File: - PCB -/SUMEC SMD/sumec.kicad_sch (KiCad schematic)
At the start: 0 parts

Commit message: PCB SMD update
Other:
- title: SUMEC THT -> SUMEC SMD
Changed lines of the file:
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@@
   (paper "A4")
   (title_block
-    (title "SUMEC THT")
+    (title "SUMEC SMD")
     (company "SPŠ NA PROSEKU")
   )

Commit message: LOGO LETSS GGOOO WOOAH YEAAAAH
holy moly logo darg wizzarddry shit, its so fire LETSS GOOO
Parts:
- added R1: R, LOGO:some magic shit (logo), symbol Device:R
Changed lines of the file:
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@@
     (company "SPŠ NA PROSEKU")
   )
-  (sheet (at 21.59 83.82) (size 69.85 46.99)
+  (symbol (lib_id "some magic shit (logo):LOGO") (at 140.97 29.21 0) (unit 1)
+    (in_bom yes) (on_board yes) (dnp no) (fields_autoplaced)
+    (property "Reference" "#G1" (at 140.97 18.5843 0)
+      (effects (font (size 1.27 1.27)) hide)
+    )
+    (property "Value" "LOGO" (at 140.97 39.8357 0)
+      (effects (font (size 1.27 1.27)) hide)
+    )
+    (property "Footprint" "LOGO:some magic shit (logo)" (at 140.97 29.21 0)
+      (effects (font (size 1.27 1.27)) hide)
+    )
+    (property "Datasheet" "" (at 140.97 29.21 0)
+      (effects (font (size 1.27 1.27)) hide)
+    )
+    (instances
+      (project "sumec"
+        (path "/fc70a1a8-ed7c-4a0f-9b1a-f23293528385"
+          (reference "#G1") (unit 1)
+        )
+      )
+    )
+  )
+  (symbol (lib_id "Device:R") (at 185.42 27.94 0) (unit 1)
+    (in_bom yes) (on_board yes) (dnp no) (fields_autoplaced)
+    (property "Reference" "R1" (at 187.96 27.305 0)
+      (effects (font (size 1.27 1.27)) (justify left))
+    )
+    (property "Value" "R" (at 187.96 29.845 0)
+      (effects (font (size 1.27 1.27)) (justify left))
+    )
+    (property "Footprint" "LOGO:some magic shit (logo)" (at 183.642 27.94 90)
+      (effects (font (size 1.27 1.27)) hide)
+    )
+    (property "Datasheet" "~" (at 185.42 27.94 0)
+      (effects (font (size 1.27 1.27)) hide)
+    )
+    (pin "1")
+    (pin "2")
+    (instances
+      (project "sumec"
+        (path "/fc70a1a8-ed7c-4a0f-9b1a-f23293528385"
+          (reference "R1") (unit 1)
+        )
+      )
+    )
+  )
+  (sheet (at 22.86 110.49) (size 69.85 46.99)
     (stroke (width 0.1524) (type solid) (color 0 0 0 1))
     (fill (color 255 255 255 1.0000))
-    (property "Sheetname" "MECHANICS" (at 33.02 110.49 0)
+    (property "Sheetname" "MECHANICS" (at 34.29 137.16 0)
       (effects (font (size 5 5) bold (color 0 0 0 1)) (justify left bottom))
     )
-    (property "Sheetfile" "MECHANICS.kicad_sch" (at 21.59 132.08 0)
+    (property "Sheetfile" "MECHANICS.kicad_sch" (at 22.86 158.75 0)
       (effects (font (size 1.27 1.27) (color 0 0 0 1)) (justify left top))
     )
@@
     )
   )
-  (sheet (at 20.32 21.59) (size 69.85 46.99)
+  (sheet (at 22.86 53.34) (size 69.85 46.99)
     (stroke (width 0.1524) (type solid) (color 0 0 0 1))
     (fill (color 255 255 255 1.0000))
-    (property "Sheetname" "MCU" (at 45.72 46.99 0)
+    (property "Sheetname" "MCU" (at 48.26 78.74 0)
       (effects (font (size 5 5) bold (color 0 0 0 1)) (justify left bottom))
     )
-    (property "Sheetfile" "MCU.kicad_sch" (at 20.32 69.85 0)
+    (property "Sheetfile" "MCU.kicad_sch" (at 22.86 101.6 0)
       (effects (font (size 1.27 1.27) (color 0 0 0 1)) (justify left top))
     )
@@
     )
   )
-  (sheet (at 196.85 21.59) (size 69.85 46.99)
+  (sheet (at 199.39 53.34) (size 69.85 46.99)
     (stroke (width 0.1524) (type solid) (color 0 0 0 1))
     (fill (color 255 255 255 1.0000))
-    (property "Sheetname" "POWER SUPPLY" (at 201.93 46.99 0)
+    (property "Sheetname" "POWER SUPPLY" (at 204.47 78.74 0)
       (effects (font (size 5 5) bold (color 0 0 0 1)) (justify left bottom))
     )
-    (property "Sheetfile" "POWER SUPPLY.kicad_sch" (at 196.85 69.85 0)
+    (property "Sheetfile" "POWER SUPPLY.kicad_sch" (at 199.39 101.6 0)
       (effects (font (size 1.27 1.27) (color 0 0 0 1)) (justify left top))
     )
@@
     )
   )
-  (sheet (at 107.95 21.59) (size 69.85 46.99)
+  (sheet (at 110.49 53.34) (size 69.85 46.99)
     (stroke (width 0.1524) (type solid) (color 0 0 0 1))
     (fill (color 255 255 255 1.0000))
-    (property "Sheetname" "SENSORS" (at 125.73 46.99 0)
+    (property "Sheetname" "SENSORS" (at 128.27 78.74 0)
       (effects (font (size 5 5) bold (color 0 0 0 1)) (justify left bottom))
     )
-    (property "Sheetfile" "SENSORS.kicad_sch" (at 107.95 69.1646 0)
+    (property "Sheetfile" "SENSORS.kicad_sch" (at 110.49 100.9146 0)
       (effects (font (size 1.27 1.27) (color 0 0 0 1)) (justify left top))
     )
-    (property "Field2" "" (at 107.95 21.59 0)
+    (property "Field2" "" (at 110.49 53.34 0)
       (effects (font (size 1.27 1.27)) hide)
     )

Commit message: PCB SMD update
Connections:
- no-connect marks 0 -> 2
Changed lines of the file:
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@@
     (company "SPŠ NA PROSEKU")
+  )
+  (no_connect (at 158.75 40.64))
+  (no_connect (at 130.81 40.64))
+  (wire (pts (xy 158.75 40.64) (xy 148.59 40.64))
+    (stroke (width 0) (type default))
+  )
+  (wire (pts (xy 130.81 40.64) (xy 140.97 40.64))
+    (stroke (width 0) (type default))
   )
   (symbol (lib_id "some magic shit (logo):LOGO") (at 140.97 29.21 0) (unit 1)
@@
     )
   )
-  (symbol (lib_id "Device:R") (at 185.42 27.94 0) (unit 1)
-    (in_bom yes) (on_board yes) (dnp no) (fields_autoplaced)
-    (property "Reference" "R1" (at 187.96 27.305 0)
-      (effects (font (size 1.27 1.27)) (justify left))
+  (symbol (lib_id "Device:R") (at 144.78 40.64 270) (mirror x) (unit 1)
+    (in_bom yes) (on_board yes) (dnp no)
+    (property "Reference" "R1" (at 145.415 38.1 0)
+      (effects (font (size 1.27 1.27)) (justify left) hide)
     )
-    (property "Value" "R" (at 187.96 29.845 0)
-      (effects (font (size 1.27 1.27)) (justify left))
+    (property "Value" "R" (at 142.875 38.1 0)
+      (effects (font (size 1.27 1.27)) (justify left) hide)
     )
-    (property "Footprint" "LOGO:some magic shit (logo)" (at 183.642 27.94 90)
+    (property "Footprint" "LOGO:some magic shit (logo)" (at 144.78 42.418 90)
       (effects (font (size 1.27 1.27)) hide)
     )
-    (property "Datasheet" "~" (at 185.42 27.94 0)
+    (property "Datasheet" "~" (at 144.78 40.64 0)
       (effects (font (size 1.27 1.27)) hide)
     )

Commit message: PCB smd - schematic update
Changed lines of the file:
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@@
     (company "SPŠ NA PROSEKU")
   )
-  (no_connect (at 158.75 40.64))
-  (no_connect (at 130.81 40.64))
-  (wire (pts (xy 158.75 40.64) (xy 148.59 40.64))
+  (no_connect (at 168.91 39.37))
+  (no_connect (at 140.97 39.37))
+  (wire (pts (xy 168.91 39.37) (xy 158.75 39.37))
     (stroke (width 0) (type default))
   )
-  (wire (pts (xy 130.81 40.64) (xy 140.97 40.64))
+  (wire (pts (xy 140.97 39.37) (xy 151.13 39.37))
     (stroke (width 0) (type default))
   )
-  (symbol (lib_id "some magic shit (logo):LOGO") (at 140.97 29.21 0) (unit 1)
+  (symbol (lib_id "some magic shit (logo):LOGO") (at 146.05 30.48 0) (unit 1)
     (in_bom yes) (on_board yes) (dnp no) (fields_autoplaced)
-    (property "Reference" "#G1" (at 140.97 18.5843 0)
+    (property "Reference" "#G1" (at 146.05 19.8543 0)
       (effects (font (size 1.27 1.27)) hide)
     )
-    (property "Value" "LOGO" (at 140.97 39.8357 0)
+    (property "Value" "LOGO" (at 146.05 41.1057 0)
       (effects (font (size 1.27 1.27)) hide)
     )
-    (property "Footprint" "LOGO:some magic shit (logo)" (at 140.97 29.21 0)
+    (property "Footprint" "LOGO:some magic shit (logo)" (at 146.05 30.48 0)
       (effects (font (size 1.27 1.27)) hide)
     )
-    (property "Datasheet" "" (at 140.97 29.21 0)
+    (property "Datasheet" "" (at 146.05 30.48 0)
       (effects (font (size 1.27 1.27)) hide)
     )
@@
     )
   )
-  (symbol (lib_id "Device:R") (at 144.78 40.64 270) (mirror x) (unit 1)
+  (symbol (lib_id "Device:R") (at 154.94 39.37 270) (mirror x) (unit 1)
     (in_bom yes) (on_board yes) (dnp no)
-    (property "Reference" "R1" (at 145.415 38.1 0)
+    (property "Reference" "R1" (at 155.575 36.83 0)
       (effects (font (size 1.27 1.27)) (justify left) hide)
     )
-    (property "Value" "R" (at 142.875 38.1 0)
+    (property "Value" "R" (at 153.035 36.83 0)
       (effects (font (size 1.27 1.27)) (justify left) hide)
     )
-    (property "Footprint" "LOGO:some magic shit (logo)" (at 144.78 42.418 90)
+    (property "Footprint" "LOGO:some magic shit (logo)" (at 154.94 41.148 90)
       (effects (font (size 1.27 1.27)) hide)
     )
-    (property "Datasheet" "~" (at 144.78 40.64 0)
+    (property "Datasheet" "~" (at 154.94 39.37 0)
       (effects (font (size 1.27 1.27)) hide)
     )
@@
     )
   )
-  (sheet (at 22.86 110.49) (size 69.85 46.99)
+  (sheet (at 27.94 107.95) (size 69.85 46.99)
     (stroke (width 0.1524) (type solid) (color 0 0 0 1))
     (fill (color 255 255 255 1.0000))
-    (property "Sheetname" "MECHANICS" (at 34.29 137.16 0)
+    (property "Sheetname" "MECHANICS" (at 39.37 134.62 0)
       (effects (font (size 5 5) bold (color 0 0 0 1)) (justify left bottom))
     )
-    (property "Sheetfile" "MECHANICS.kicad_sch" (at 22.86 158.75 0)
+    (property "Sheetfile" "MECHANICS.kicad_sch" (at 27.94 156.21 0)
       (effects (font (size 1.27 1.27) (color 0 0 0 1)) (justify left top))
     )
@@
     )
   )
-  (sheet (at 22.86 53.34) (size 69.85 46.99)
+  (sheet (at 27.94 49.53) (size 69.85 46.99)
     (stroke (width 0.1524) (type solid) (color 0 0 0 1))
     (fill (color 255 255 255 1.0000))
-    (property "Sheetname" "MCU" (at 48.26 78.74 0)
+    (property "Sheetname" "MCU" (at 53.34 74.93 0)
       (effects (font (size 5 5) bold (color 0 0 0 1)) (justify left bottom))
     )
-    (property "Sheetfile" "MCU.kicad_sch" (at 22.86 101.6 0)
+    (property "Sheetfile" "MCU.kicad_sch" (at 27.94 97.79 0)
       (effects (font (size 1.27 1.27) (color 0 0 0 1)) (justify left top))
     )
@@
     )
   )
-  (sheet (at 199.39 53.34) (size 69.85 46.99)
+  (sheet (at 204.47 49.53) (size 69.85 46.99)
     (stroke (width 0.1524) (type solid) (color 0 0 0 1))
     (fill (color 255 255 255 1.0000))
-    (property "Sheetname" "POWER SUPPLY" (at 204.47 78.74 0)
+    (property "Sheetname" "POWER SUPPLY" (at 209.55 74.93 0)
       (effects (font (size 5 5) bold (color 0 0 0 1)) (justify left bottom))
     )
-    (property "Sheetfile" "POWER SUPPLY.kicad_sch" (at 199.39 101.6 0)
+    (property "Sheetfile" "POWER SUPPLY.kicad_sch" (at 204.47 97.79 0)
       (effects (font (size 1.27 1.27) (color 0 0 0 1)) (justify left top))
     )
@@
     )
   )
-  (sheet (at 110.49 53.34) (size 69.85 46.99)
+  (sheet (at 115.57 49.53) (size 69.85 46.99)
     (stroke (width 0.1524) (type solid) (color 0 0 0 1))
     (fill (color 255 255 255 1.0000))
-    (property "Sheetname" "SENSORS" (at 128.27 78.74 0)
+    (property "Sheetname" "SENSORS" (at 133.35 74.93 0)
       (effects (font (size 5 5) bold (color 0 0 0 1)) (justify left bottom))
     )
-    (property "Sheetfile" "SENSORS.kicad_sch" (at 110.49 100.9146 0)
+    (property "Sheetfile" "SENSORS.kicad_sch" (at 115.57 97.1046 0)
       (effects (font (size 1.27 1.27) (color 0 0 0 1)) (justify left top))
     )
-    (property "Field2" "" (at 110.49 53.34 0)
+    (property "Field2" "" (at 115.57 49.53 0)
       (effects (font (size 1.27 1.27)) hide)
     )

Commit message: PCB update
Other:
- added sheet EXTERNAL (EXTERNAL.kicad_sch)
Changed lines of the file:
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@@
     )
   )
-  (sheet (at 27.94 107.95) (size 69.85 46.99)
+  (sheet (at 27.94 106.68) (size 69.85 46.99)
     (stroke (width 0.1524) (type solid) (color 0 0 0 1))
     (fill (color 255 255 255 1.0000))
-    (property "Sheetname" "MECHANICS" (at 39.37 134.62 0)
+    (property "Sheetname" "MECHANICS" (at 39.37 133.35 0)
       (effects (font (size 5 5) bold (color 0 0 0 1)) (justify left bottom))
     )
-    (property "Sheetfile" "MECHANICS.kicad_sch" (at 27.94 156.21 0)
+    (property "Sheetfile" "MECHANICS.kicad_sch" (at 27.94 154.94 0)
       (effects (font (size 1.27 1.27) (color 0 0 0 1)) (justify left top))
     )
@@
     )
   )
-  (sheet (at 27.94 49.53) (size 69.85 46.99)
+  (sheet (at 27.94 48.26) (size 69.85 46.99)
     (stroke (width 0.1524) (type solid) (color 0 0 0 1))
     (fill (color 255 255 255 1.0000))
-    (property "Sheetname" "MCU" (at 53.34 74.93 0)
+    (property "Sheetname" "MCU" (at 53.34 73.66 0)
       (effects (font (size 5 5) bold (color 0 0 0 1)) (justify left bottom))
     )
-    (property "Sheetfile" "MCU.kicad_sch" (at 27.94 97.79 0)
+    (property "Sheetfile" "MCU.kicad_sch" (at 27.94 96.52 0)
       (effects (font (size 1.27 1.27) (color 0 0 0 1)) (justify left top))
     )
@@
     )
   )
-  (sheet (at 204.47 49.53) (size 69.85 46.99)
+  (sheet (at 204.47 48.26) (size 69.85 46.99)
     (stroke (width 0.1524) (type solid) (color 0 0 0 1))
     (fill (color 255 255 255 1.0000))
-    (property "Sheetname" "POWER SUPPLY" (at 209.55 74.93 0)
+    (property "Sheetname" "POWER SUPPLY" (at 209.55 73.66 0)
       (effects (font (size 5 5) bold (color 0 0 0 1)) (justify left bottom))
     )
-    (property "Sheetfile" "POWER SUPPLY.kicad_sch" (at 204.47 97.79 0)
+    (property "Sheetfile" "POWER SUPPLY.kicad_sch" (at 204.47 96.52 0)
       (effects (font (size 1.27 1.27) (color 0 0 0 1)) (justify left top))
     )
@@
     )
   )
-  (sheet (at 115.57 49.53) (size 69.85 46.99)
+  (sheet (at 115.57 48.26) (size 69.85 46.99)
     (stroke (width 0.1524) (type solid) (color 0 0 0 1))
     (fill (color 255 255 255 1.0000))
-    (property "Sheetname" "SENSORS" (at 133.35 74.93 0)
+    (property "Sheetname" "SENSORS" (at 133.35 73.66 0)
       (effects (font (size 5 5) bold (color 0 0 0 1)) (justify left bottom))
     )
-    (property "Sheetfile" "SENSORS.kicad_sch" (at 115.57 97.1046 0)
+    (property "Sheetfile" "SENSORS.kicad_sch" (at 115.57 95.8346 0)
       (effects (font (size 1.27 1.27) (color 0 0 0 1)) (justify left top))
     )
-    (property "Field2" "" (at 115.57 49.53 0)
+    (property "Field2" "" (at 115.57 48.26 0)
       (effects (font (size 1.27 1.27)) hide)
     )
@@
       )
     )
+  )
+  (sheet (at 115.57 106.68) (size 69.85 46.99)
+    (stroke (width 0.1524) (type solid) (color 0 0 0 1))
+    (fill (color 255 255 255 1.0000))
+    (property "Sheetname" "EXTERNAL" (at 132.08 133.35 0)
+      (effects (font (size 5 5) bold (color 0 0 0 1)) (justify left bottom))
+    )
+    (property "Sheetfile" "EXTERNAL.kicad_sch" (at 115.57 154.2546 0)
+      (effects (font (size 1.27 1.27) (color 0 0 0 1)) (justify left top))
+    )
+    (instances
+      (project "sumec"
+        (path "/fc70a1a8-ed7c-4a0f-9b1a-f23293528385" (page "6"))
+      )
+    )

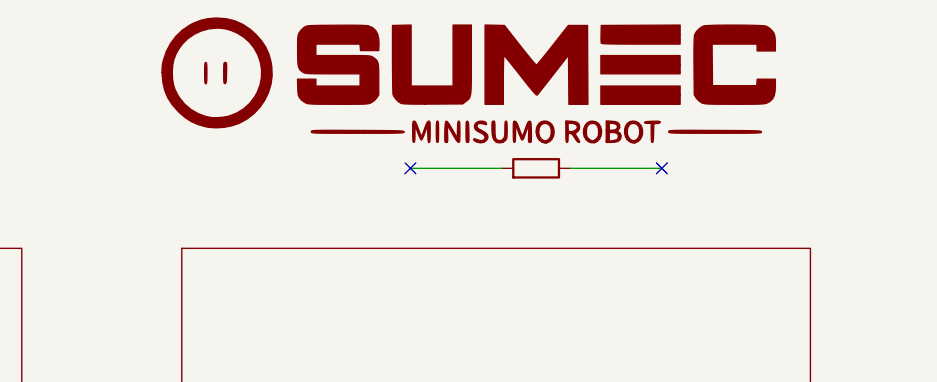
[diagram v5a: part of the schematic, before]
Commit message: PCB Update - "LIDAR"sensors
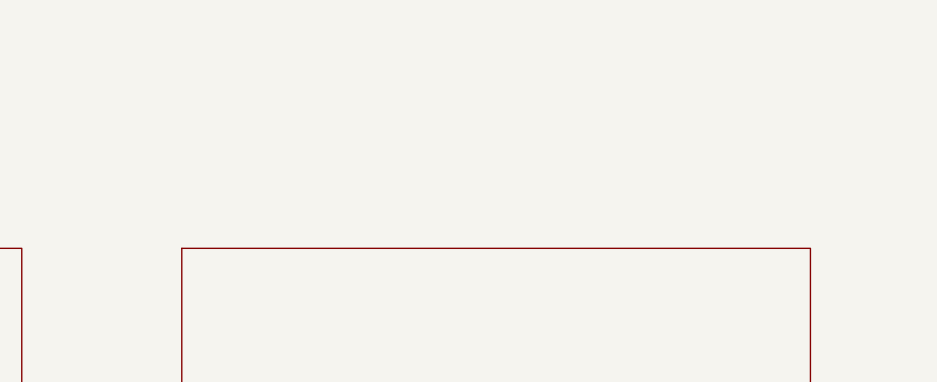
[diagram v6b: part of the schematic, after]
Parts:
- removed R1: R, LOGO:some magic shit (logo), symbol Device:R
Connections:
- no-connect marks 2 -> 0
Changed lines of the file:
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@@
     (company "SPŠ NA PROSEKU")
-  )
-  (no_connect (at 168.91 39.37))
-  (no_connect (at 140.97 39.37))
-  (wire (pts (xy 168.91 39.37) (xy 158.75 39.37))
-    (stroke (width 0) (type default))
-  )
-  (wire (pts (xy 140.97 39.37) (xy 151.13 39.37))
-    (stroke (width 0) (type default))
-  )
-  (symbol (lib_id "some magic shit (logo):LOGO") (at 146.05 30.48 0) (unit 1)
-    (in_bom yes) (on_board yes) (dnp no) (fields_autoplaced)
-    (property "Reference" "#G1" (at 146.05 19.8543 0)
-      (effects (font (size 1.27 1.27)) hide)
-    )
-    (property "Value" "LOGO" (at 146.05 41.1057 0)
-      (effects (font (size 1.27 1.27)) hide)
-    )
-    (property "Footprint" "LOGO:some magic shit (logo)" (at 146.05 30.48 0)
-      (effects (font (size 1.27 1.27)) hide)
-    )
-    (property "Datasheet" "" (at 146.05 30.48 0)
-      (effects (font (size 1.27 1.27)) hide)
-    )
-    (instances
-      (project "sumec"
-        (path "/fc70a1a8-ed7c-4a0f-9b1a-f23293528385"
-          (reference "#G1") (unit 1)
-        )
-      )
-    )
-  )
-  (symbol (lib_id "Device:R") (at 154.94 39.37 270) (mirror x) (unit 1)
-    (in_bom yes) (on_board yes) (dnp no)
-    (property "Reference" "R1" (at 155.575 36.83 0)
-      (effects (font (size 1.27 1.27)) (justify left) hide)
-    )
-    (property "Value" "R" (at 153.035 36.83 0)
-      (effects (font (size 1.27 1.27)) (justify left) hide)
-    )
-    (property "Footprint" "LOGO:some magic shit (logo)" (at 154.94 41.148 90)
-      (effects (font (size 1.27 1.27)) hide)
-    )
-    (property "Datasheet" "~" (at 154.94 39.37 0)
-      (effects (font (size 1.27 1.27)) hide)
-    )
-    (pin "1")
-    (pin "2")
-    (instances
-      (project "sumec"
-        (path "/fc70a1a8-ed7c-4a0f-9b1a-f23293528385"
-          (reference "R1") (unit 1)
-        )
-      )
-    )
   )
   (sheet (at 27.94 106.68) (size 69.85 46.99)

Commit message: pcb update cleanup
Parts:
- added R1: R, sumec-smd_library:logo small, symbol Device:R
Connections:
- no-connect marks 0 -> 2
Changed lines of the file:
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@@
     (company "SPŠ NA PROSEKU")
+  )
+  (no_connect (at 128.27 36.83))
+  (no_connect (at 177.8 36.83))
+  (wire (pts (xy 128.27 36.83) (xy 148.59 36.83))
+    (stroke (width 0) (type default))
+  )
+  (wire (pts (xy 177.8 36.83) (xy 156.21 36.83))
+    (stroke (width 0) (type default))
+  )
+  (symbol (lib_id "some magic shit (logo):LOGO") (at 144.78 26.67 0) (unit 1)
+    (in_bom yes) (on_board yes) (dnp no) (fields_autoplaced)
+    (property "Reference" "#G1" (at 144.78 16.0443 0)
+      (effects (font (size 1.27 1.27)) hide)
+    )
+    (property "Value" "LOGO" (at 144.78 37.2957 0)
+      (effects (font (size 1.27 1.27)) hide)
+    )
+    (property "Footprint" "" (at 144.78 26.67 0)
+      (effects (font (size 1.27 1.27)) hide)
+    )
+    (property "Datasheet" "" (at 144.78 26.67 0)
+      (effects (font (size 1.27 1.27)) hide)
+    )
+    (instances
+      (project "sumec"
+        (path "/fc70a1a8-ed7c-4a0f-9b1a-f23293528385"
+          (reference "#G1") (unit 1)
+        )
+      )
+    )
+  )
+  (symbol (lib_id "Device:R") (at 152.4 36.83 90) (unit 1)
+    (in_bom yes) (on_board yes) (dnp no) (fields_autoplaced)
+    (property "Reference" "R1" (at 152.4 31.75 90)
+      (effects (font (size 1.27 1.27)) hide)
+    )
+    (property "Value" "R" (at 152.4 34.29 90)
+      (effects (font (size 1.27 1.27)) hide)
+    )
+    (property "Footprint" "sumec-smd_library:logo small" (at 152.4 38.608 90)
+      (effects (font (size 1.27 1.27)) hide)
+    )
+    (property "Datasheet" "~" (at 152.4 36.83 0)
+      (effects (font (size 1.27 1.27)) hide)
+    )
+    (pin "1")
+    (pin "2")
+    (instances
+      (project "sumec"
+        (path "/fc70a1a8-ed7c-4a0f-9b1a-f23293528385"
+          (reference "R1") (unit 1)
+        )
+      )
+    )
   )
   (sheet (at 27.94 106.68) (size 69.85 46.99)

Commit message: i desire sleep
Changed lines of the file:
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@@
     (company "SPŠ NA PROSEKU")
   )
-  (no_connect (at 128.27 36.83))
-  (no_connect (at 177.8 36.83))
-  (wire (pts (xy 128.27 36.83) (xy 148.59 36.83))
+  (no_connect (at 127 36.83))
+  (no_connect (at 180.34 36.83))
+  (wire (pts (xy 127 36.83) (xy 149.86 36.83))
     (stroke (width 0) (type default))
   )
-  (wire (pts (xy 177.8 36.83) (xy 156.21 36.83))
+  (wire (pts (xy 180.34 36.83) (xy 157.48 36.83))
     (stroke (width 0) (type default))
   )
@@
     )
   )
-  (symbol (lib_id "Device:R") (at 152.4 36.83 90) (unit 1)
+  (symbol (lib_id "Device:R") (at 153.67 36.83 90) (unit 1)
     (in_bom yes) (on_board yes) (dnp no) (fields_autoplaced)
-    (property "Reference" "R1" (at 152.4 31.75 90)
+    (property "Reference" "R1" (at 153.67 31.75 90)
       (effects (font (size 1.27 1.27)) hide)
     )
-    (property "Value" "R" (at 152.4 34.29 90)
+    (property "Value" "R" (at 153.67 34.29 90)
       (effects (font (size 1.27 1.27)) hide)
     )
-    (property "Footprint" "sumec-smd_library:logo small" (at 152.4 38.608 90)
+    (property "Footprint" "sumec-smd_library:logo small" (at 153.67 38.608 90)
       (effects (font (size 1.27 1.27)) hide)
     )
-    (property "Datasheet" "~" (at 152.4 36.83 0)
+    (property "Datasheet" "~" (at 153.67 36.83 0)
       (effects (font (size 1.27 1.27)) hide)
     )
